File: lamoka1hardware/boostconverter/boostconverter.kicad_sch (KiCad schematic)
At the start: 39 parts, among them Q1 NMOS

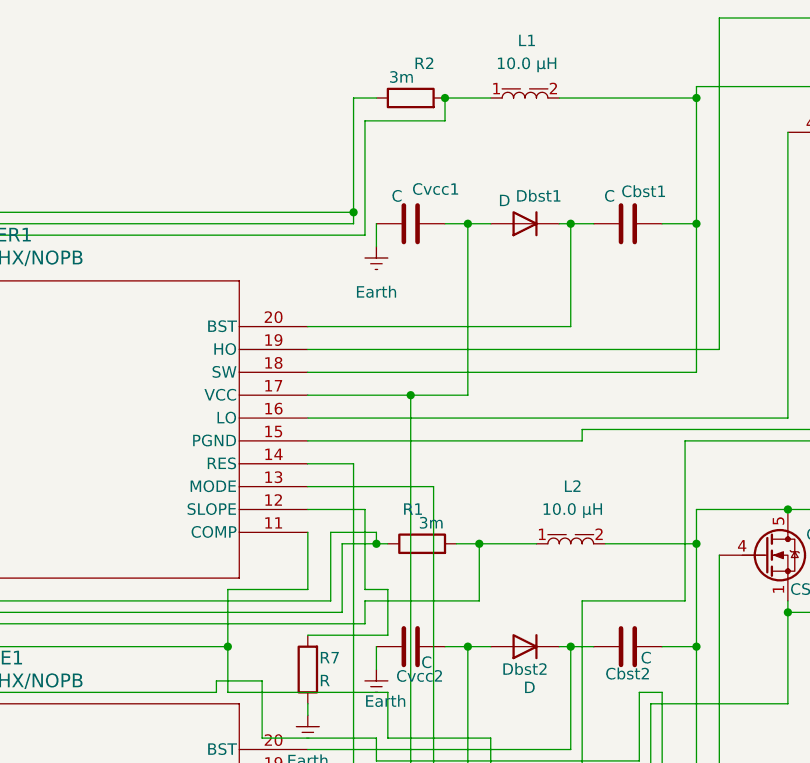
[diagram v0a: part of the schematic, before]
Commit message: ADD footprints for items
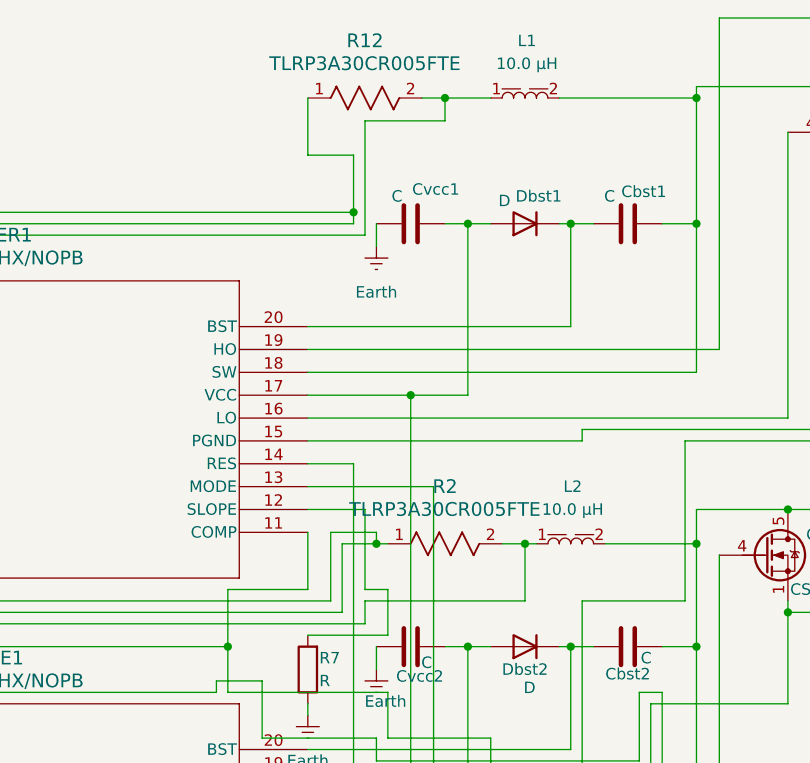
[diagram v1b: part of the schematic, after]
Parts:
- removed R1, R2: 3m, symbol Device:R
- added R12, R2: TLRP3A30CR005FTE, current sense:RES_TLRP-3A_TEC, symbol 2026-06-21_01-10-03:TLRP3A30CR005FTE
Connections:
- net at Cin1.1, Cin2.1, Cin3.1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: now also R12.1, R2.1
- net at L1.1, MASTER1.3 (CSN): now also R12.2
- net at L2.1, SLAVE1.3 (CSN): now also R2.2

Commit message: ADD some better foot printing, better documentation
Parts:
- MASTER1, SLAVE1: value LM5122QMHX/NOPB -> LM5122QMHE/NOPB; footprint footprints:PWP20_3P0X4P2 -> LM5122:PWP0020A_M
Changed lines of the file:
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@@
 			)
 		)
-		(property "Value" "LM5122QMHX/NOPB"
+		(property "Value" "LM5122QMHE/NOPB"
 			(at 128.27 45.72 0)
 			(show_name no)
@@
 			)
 		)
-		(property "Footprint" "footprints:PWP20_3P0X4P2"
+		(property "Footprint" "LM5122:PWP0020A_M"
 			(at 92.71 53.34 0)
 			(hide yes)
@@
 			)
 		)
-		(property "Value" "LM5122QMHX/NOPB"
+		(property "Value" "LM5122QMHE/NOPB"
 			(at 128.27 92.71 0)
 			(show_name no)
@@
 			)
 		)
-		(property "Footprint" "footprints:PWP20_3P0X4P2"
+		(property "Footprint" "LM5122:PWP0020A_M"
 			(at 92.71 100.33 0)
 			(hide yes)

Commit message: ADD alot of work (I dont even remember what i did lol)
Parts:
- removed Cin1, Cin2, Cin3, Cout1, Cout2, Cout3: C, symbol Device:C
- removed Dbst1, Dbst2: D, symbol Device:D
- added C1, C4: UCD2A220MNL1GS, incapsmall:PCAP_8x10-ELECT_NCH, symbol 2026-06-22_18-02-40:UCD2A220MNL1GS
- added C2, C3: UUX2A470MNL1GS, footprint:PCAP_10x10-ELECT_NCA, symbol dos input caps:UUX2A470MNL1GS
- added C5: KRM55WR72A226MH01L, KRM55WR72A226MH01L-kicadfiles:CAPC6153X670N, symbol KRM55WR72A226MH01L:KRM55WR72A226MH01L
- added C6: UCD2A101MNJ1MS, footprint3:CAP_UCD2A_NCH, symbol 2026-06-23_14-35-42:UCD2A101MNJ1MS
- added IC1, IC2: SDM1U100S1F-7, SDM1U100S1F-7-kicadfiles:SODFL3518X115N, symbol SDM1U100S1F-7:SDM1U100S1F-7
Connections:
- net Earth: now also C1.2, C2.2, C3.2, C4.2, C5.1, C6.1
- net at Cvcc1.2, MASTER1.17 (VCC), R5.1: now also IC1.2 (A)
- net at Cbst1.1, MASTER1.20 (BST): now also IC1.1 (K)
- net at MASTER1.4 (CSP), MASTER1.5 (VIN), R12.1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: now also C1.1, C2.1, C3.1
- net at Qh1.5 (D), Qh2.5 (D), R10.1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: now also C4.1, C5.2, C6.2
- net at Cbst2.1, SLAVE1.20 (BST): now also IC2.1 (K)
- net at Cvcc2.2, SLAVE1.10 (FB), SLAVE1.17 (VCC): now also IC2.2 (A)
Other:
- moved on the sheet: L1, L2

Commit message: ADD alot of random stuff (footprints, etc)
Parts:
- removed Cbst1, Cbst2, Css1, Cvcc1, Cvcc2: C, symbol Device:C
- removed R6, R7: R, symbol Device:R
- removed R8: 36k, symbol Device:R
- added C11: CL10B104KB8NNNC, footprint989:CAP_CL10_SAM, symbol 2026-06-24_20-27-18:CL10B104KB8NNNC
- added Cbst1, Cbst2: C1206C224M1REC7210, footprints:CAP_C1206C-EC_KEM, symbol 2026-06-24_23-31-22:C1206C224M1REC7210
- added Cvcc1, Cvcc2: CNC5L1X7R1H106K160AE, CNC5L1X7R1H106K160AE-kicadfiles:CAPC3216X190N, symbol CNC5L1X7R1H106K160AE:CNC5L1X7R1H106K160AE
- added R13, R14, R7: RC0603FR-0736KL, footprint9:RC0603N_YAG, symbol 2026-06-24_19-49-47:RC0603FR-0736KL
- renumbered IC1 to Dbst1, IC2 to Dbst2
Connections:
- net Earth: now also C11.1, Cvcc1.1, Cvcc2.1, R13.2, R14.2, R7.1
- net at Dbst2.1 (K), SLAVE1.20 (BST): now also Cbst2.1
- net at Dbst2.2 (A), SLAVE1.10 (FB), SLAVE1.17 (VCC): now also Cvcc2.2
- net at MASTER1.12 (SLOPE): now also R13.1
- net at Dbst1.2 (A), MASTER1.17 (VCC), R5.1: now also Cvcc1.2
- net at L1.2, MASTER1.18 (SW), Qh1.1 (S)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: now also Cbst1.2
- net at Dbst1.1 (K), MASTER1.20 (BST): now also Cbst1.1
- net at MASTER1.7 (SS), SLAVE1.7 (SS): now also C11.2
- net at MASTER1.8 (SYNCIN/RT): now also R14.1
- net at L2.2, Qh2.1 (S), Qh2.2 (S)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: now also Cbst2.2
- net at SLAVE1.12 (SLOPE): now also R7.2
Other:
- moved on the sheet: Q1, SIGM1
